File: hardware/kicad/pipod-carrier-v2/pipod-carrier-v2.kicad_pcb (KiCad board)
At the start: 2 copper layers, 65 x 110 mm, 17 parts, among them J1 Raspberry_Pi_Zero_2W, J3 Conn_02x06_Odd_Even, J5 Conn_01x02, SW1 Volume Up, SW2 Volume Down, SW3 PWR, U1 Adafruit Seesaw Encoder, U3 PCM5102A, U4 TPA6132

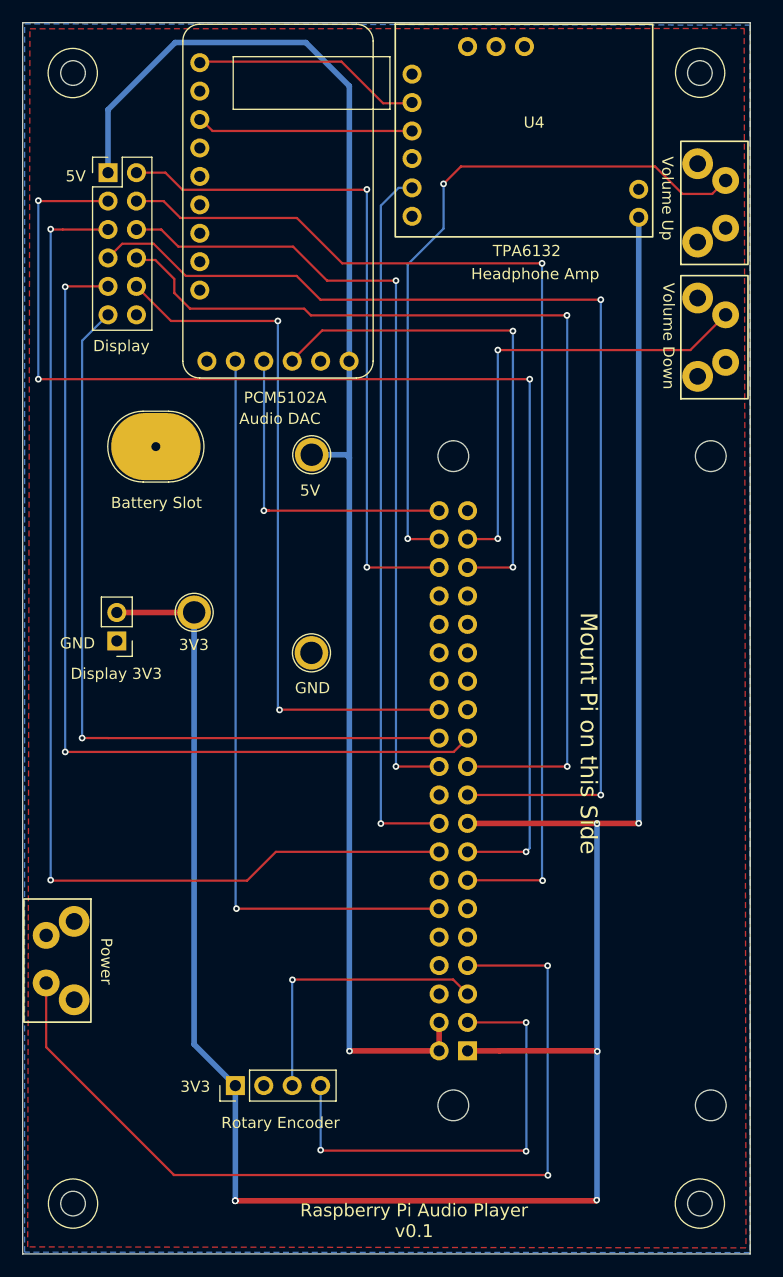
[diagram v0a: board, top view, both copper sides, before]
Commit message: fixed PCB battery slot and mounting hole diameters
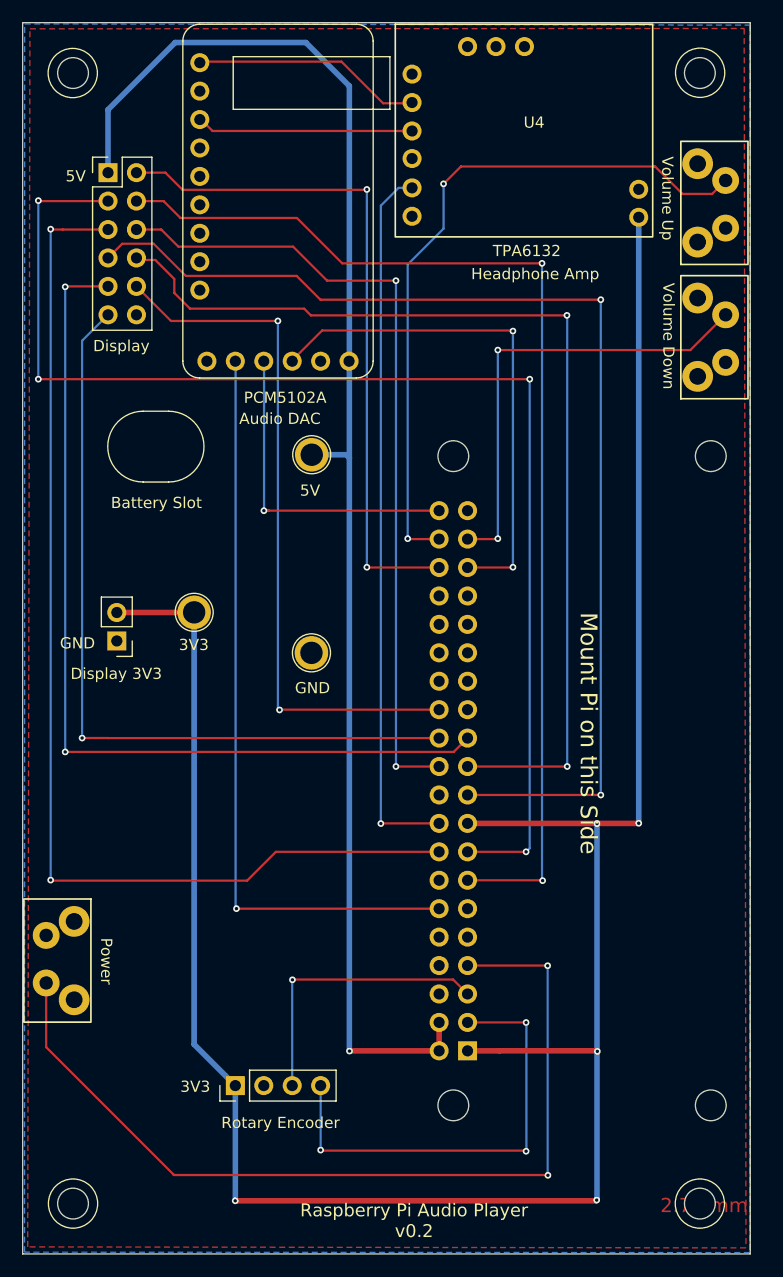
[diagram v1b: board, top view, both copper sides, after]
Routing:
- net /3V3: vias 6 -> 5
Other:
- board text added: "2.75 mm"
- board text added: "Raspberry Pi Audio Player v0.2"
- board text removed: "Raspberry Pi Audio Player v0.1"
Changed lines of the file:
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@@
 			(at 0 7.5)
 			(size 8 6)
-			(drill 0.8)
+			(drill oval 8 6)
 			(layers "*.Cu" "*.Mask")
 		)
@@
 		(pad "" np_thru_hole circle
 			(at 0 0)
-			(size 2.2 2.2)
-			(drill 2.2)
+			(size 2.75 2.75)
+			(drill 2.75)
 			(layers "*.Cu" "*.Mask")
 		)
@@
 		(pad "" np_thru_hole circle
 			(at 0 0)
-			(size 2.2 2.2)
-			(drill 2.2)
+			(size 2.75 2.75)
+			(drill 2.75)
 			(layers "*.Cu" "*.Mask")
 		)
@@
 		(pad "" np_thru_hole circle
 			(at 0 0)
-			(size 2.2 2.2)
-			(drill 2.2)
+			(size 2.75 2.75)
+			(drill 2.75)
 			(layers "*.Cu" "*.Mask")
 		)
@@
 		(pad "" np_thru_hole circle
 			(at 0 0.025)
-			(size 2.2 2.2)
-			(drill 2.2)
+			(size 2.75 2.75)
+			(drill 2.75)
 			(layers "*.Cu" "*.Mask")
 		)
@@
 		(layer "Edge.Cuts")
 	)
+	(gr_text "2.75 mm"
+		(at 160.875 145.875 0)
+		(layer "F.Cu")
+		(effects
+			(font
+				(size 1.27 1.27)
+			)
+		)
+	)
 	(gr_text "Display 3V3"
 		(at 104.275 98.95 0)
@@
 		)
 	)
-	(gr_text "Raspberry Pi Audio Player\nv0.1"
+	(gr_text "Raspberry Pi Audio Player\nv0.2"
 		(at 134.97 148.83 0)
 		(layer "F.SilkS")
@@
 		(size 0.6)
 		(drill 0.3)
-		(layers "F.Cu" "B.Cu")
-		(net "/3V3")
-	)
-	(via
-		(at 118.99 145.45)
-		(size 0.6)
-		(drill 0.3)

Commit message: fixed CE0 and CE1 and button 2 and button 4 labels
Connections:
- J1 pad 13: /TFT_BTN2 -> /TFT_BTN4
- J1 pad 15: /TFT_BTN4 -> /TFT_BTN2
- J1 pad 24: /TFT_CE1 -> /TFT_CE0
- J1 pad 26: /TFT_CE0 -> /TFT_CE1
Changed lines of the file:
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@@
 			(layers "*.Cu" "*.Mask")
 			(remove_unused_layers no)
-			(net "/TFT_BTN2")
+			(net "/TFT_BTN4")
 			(pinfunction "GPIO27_13")
 			(pintype "bidirectional")
@@
 			(layers "*.Cu" "*.Mask")
 			(remove_unused_layers no)
-			(net "/TFT_BTN4")
+			(net "/TFT_BTN2")
 			(pinfunction "GPIO22_15")
 			(pintype "bidirectional")
@@
 			(layers "*.Cu" "*.Mask")
 			(remove_unused_layers no)
-			(net "/TFT_CE1")
+			(net "/TFT_CE0")
 			(pinfunction "GPIO8_/_CE0_24")
 			(pintype "bidirectional")
@@
 			(layers "*.Cu" "*.Mask")
 			(remove_unused_layers no)
-			(net "/TFT_CE0")
+			(net "/TFT_CE1")
 			(pinfunction "GPIO7_/_CE1_26")
 			(pintype "bidirectional")
